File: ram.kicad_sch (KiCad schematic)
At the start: 7 parts, among them U1 LFE5U-85F-6BG381C, U2 IS42S16160J-6BL

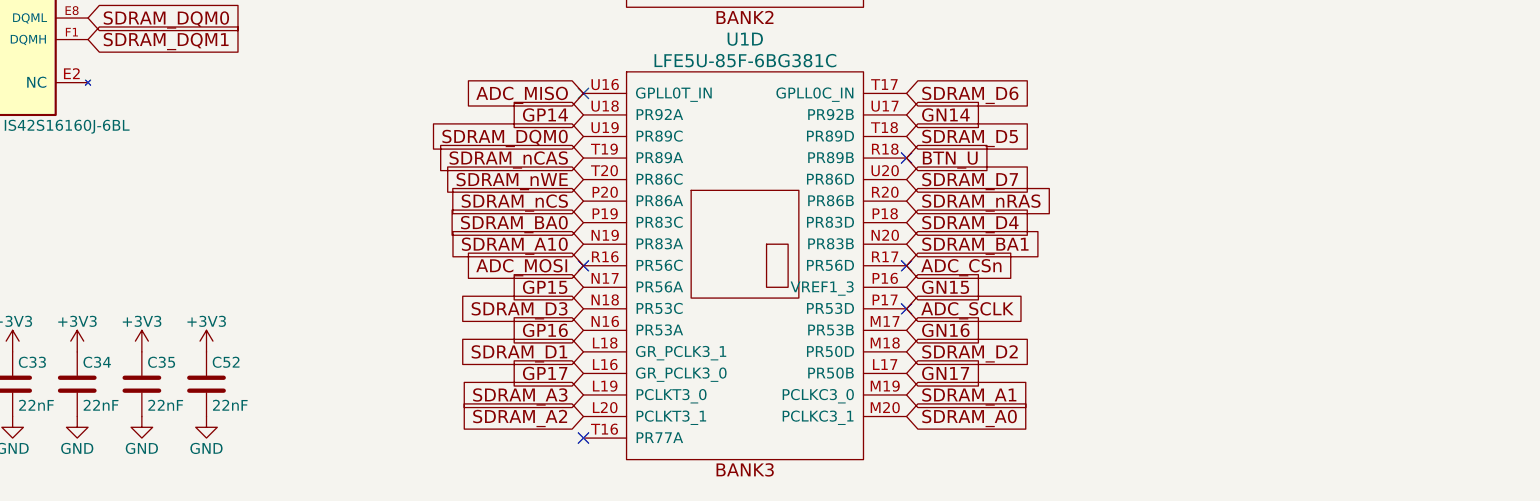
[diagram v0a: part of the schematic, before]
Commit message: add i2c header
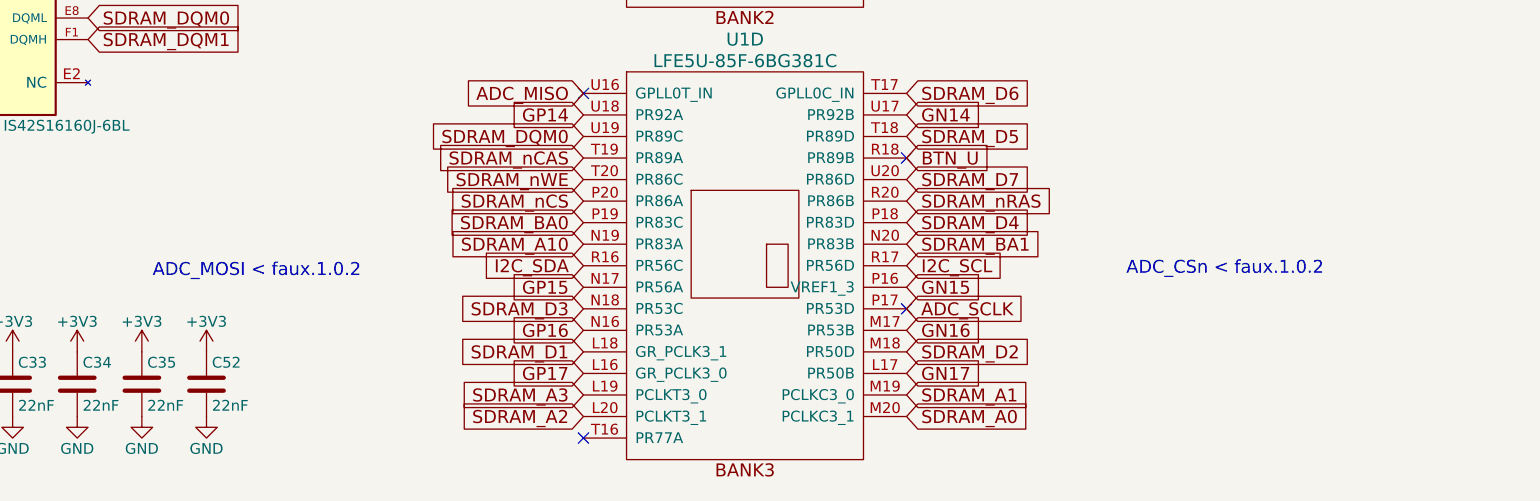
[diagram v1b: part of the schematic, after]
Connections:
- net ADC_CSn renamed I2C_SCL
- net ADC_MOSI renamed I2C_SDA
- no-connect marks 12 -> 10
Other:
- note added: "ADC_CSn < faux.1.0.2"
- note added: "ADC_MOSI < faux.1.0.2"
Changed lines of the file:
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@@
 		(comment 1 "SDRAM memory")
+	)
+	(text "ADC_MOSI < faux.1.0.2"
+		(exclude_from_sim no)
+		(at 166.37 137.414 0)
+		(effects
+			(font
+				(size 1.524 1.524)
+			)
+			(justify left bottom)
+		)
+	)
+	(text "ADC_CSn < faux.1.0.2"
+		(exclude_from_sim no)
+		(at 281.178 137.16 0)
+		(effects
+			(font
+				(size 1.524 1.524)
+			)
+			(justify left bottom)
+		)
 	)
 	(junction
@@
 	)
 	(no_connect
-		(at 255.27 135.89)
-	)
-	(no_connect
-		(at 217.17 135.89)
-	)
-	(no_connect
 		(at 255.27 87.63)
 	)
@@
 		)
 	)
-	(global_label "ADC_MOSI"
+	(global_label "I2C_SDA"
 		(shape input)
 		(at 217.17 135.89 180)
@@
 		)
 	)
-	(global_label "ADC_CSn"
+	(global_label "I2C_SCL"
 		(shape input)
 		(at 255.27 135.89 0)

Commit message: make MPN reflect mouser part numbers
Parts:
- C16: MPN CC0805MRX5R6BB225 -> 603-CC805MRX5R6BB225
- C33, C34, C35, C52: MPN CC0603JRX7R8BB223 -> 603-CC603JRX7R8BB223
- U1: MPN LFE5U-85F-6BG381C -> 842-LFE5U85F6BG381C
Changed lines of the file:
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@@
 			)
 		)
-		(property "MPN" "CC0805MRX5R6BB225"
+		(property "MPN" "603-CC805MRX5R6BB225"
 			(at 135.89 149.86 0)
 			(hide yes)
@@
 			)
 		)
-		(property "MPN" "LFE5U-85F-6BG381C"
+		(property "MPN" "842-LFE5U85F6BG381C"
 			(at 236.22 80.01 0)
 			(hide yes)
@@
 			)
 		)
-		(property "MPN" "LFE5U-85F-6BG381C"
+		(property "MPN" "842-LFE5U85F6BG381C"
 			(at 236.22 133.35 0)
 			(hide yes)
@@
 			)
 		)
-		(property "MPN" "CC0603JRX7R8BB223"
+		(property "MPN" "603-CC603JRX7R8BB223"
 			(at 149.86 149.86 0)
 			(hide yes)
@@
 			)
 		)
-		(property "MPN" "CC0603JRX7R8BB223"
+		(property "MPN" "603-CC603JRX7R8BB223"
 			(at 157.48 149.86 0)
 			(hide yes)
@@
 			)
 		)
-		(property "MPN" "CC0603JRX7R8BB223"
+		(property "MPN" "603-CC603JRX7R8BB223"
 			(at 165.1 149.86 0)
 			(hide yes)
@@
 			)
 		)
-		(property "MPN" "CC0603JRX7R8BB223"
+		(property "MPN" "603-CC603JRX7R8BB223"
 			(at 172.72 149.86 0)
 			(hide yes)
